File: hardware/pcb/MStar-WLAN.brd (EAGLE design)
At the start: 73.7 x 53.7 mm, 41 parts, among them J1 6P6C, J3 ZX62R-B-5P(30), Q1 VP2106, Q2 2N3904

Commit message: pcb
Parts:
- removed 3.3--5V: (no value), jumper:SJ_2
- removed D3: (no value), diode:D-5
- removed R8, R9: 10K, rcl:0207/2V
- C1: value 470u/25 -> 2m/25; device rcl:E3,5-8 -> rcl:E5-10,5
- C2: value 1m/6.3 -> 100u/6.3; device rcl:E5-10,5 -> rcl:E2,5-6
- moved C9 7.18 mm to (38.1, 10.2), turned to 90 degrees
- moved R4 5.24 mm to (49.5, 10.2)
- moved R7 5.24 mm to (41.9, 10.2)
- moved R3 5.08 mm to (53.3, 10.2)
- moved C10 5.08 mm to (45.7, 10.2)
- moved C1 4.02 mm to (19.1, 6.35)
- moved C2 2.84 mm to (33.7, 10.2)
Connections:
- removed net N$16: 3.3--5V.1, D3.A
- removed net N$20: 3.3--5V.2, C2.+, C3.1, OKI-78SR-3.3.OUT
- removed net N$8: ESP32-WROVER-B.4, R8.1, R9.2
- net GND: no longer R9.1
- net N$17: no longer D3.C
- net VCC: now also C2.+, C3.1, OKI-78SR-3.3.OUT; no longer 3.3--5V.3, R8.2
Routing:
- net N$20: track 50.7 -> 0.00 mm
- net N$8: track 20.9 -> 0.00 mm
- net N$16: track 16.5 -> 0.00 mm
- net ESP32_EN: track 82.6 -> 69.8 mm
- net TXD: track 44.3 -> 37.8 mm
- net N$2: track 110.7 -> 115.5 mm
- net N$7: track 14.0 -> 9.23 mm
- net VCC: track 191.4 -> 195.3 mm
- net SQW: track 114.3 -> 117.3 mm
- net N$4: track 7.86 -> 4.96 mm
- net RAW12: track 19.9 -> 17.7 mm
- net GND: track 1.74 -> 3.78 mm, vias 8 -> 10
- net N$17: track 9.81 -> 7.91 mm
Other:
- board text added: "MStar-WLAN mjs 2019.12"
- board text removed: "MStar-WLAN mjs 2019.5"

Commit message: ESP32 work
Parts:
- added C11: 10u, rcl:C1206
- added SD: (no value), con-lsta:FE06
- moved R1 8.08 mm to (5.71, 36.8), turned to 180 degrees
- moved Q1 4.07 mm to (50.2, 45.7)
- moved Q2 4.07 mm to (43.8, 45.7)
- moved R2 1.27 mm to (40.6, 50.2)
- moved R5 1.27 mm to (53.3, 50.2)
- moved R6 1.27 mm to (47.0, 50.2)
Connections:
- new net N$16: ESP32-WROVER-B.29, SD.2
- new net N$20: ESP32-WROVER-B.30, SD.4
- new net N$22: ESP32-WROVER-B.37, SD.3
- new net N$8: ESP32-WROVER-B.31, SD.5
- net GND: now also C11.2, SD.6
- net RX_ENA: now also ESP32-WROVER-B.10; no longer ESP32-WROVER-B.37
- net VCC: now also C11.1, SD.1
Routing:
- net I2C_SCL: track 138.1 -> 63.8 mm, vias 1 -> 3
- net N$2: track 115.5 -> 67.1 mm
- net SQW: track 117.3 -> 85.3 mm
- net N$22: track 0.00 -> 21.0 mm
- net /MBUS: track 52.2 -> 72.9 mm
- net VCC: track 195.3 -> 175.9 mm
- net N$19: track 74.9 -> 61.6 mm, vias 0 -> 2
- net RX_ENA: track 45.3 -> 56.2 mm, vias 1 -> 2
- net N$16: track 0.00 -> 10.6 mm
- net ESP32_EN: track 69.8 -> 61.2 mm
- net RXD: track 52.8 -> 61.1 mm, vias 3 -> 2
- net N$13: track 15.8 -> 22.8 mm
- net N$20: track 0.00 -> 6.99 mm
- net N$8: track 0.00 -> 6.47 mm
- net /RTS: track 15.3 -> 9.87 mm
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
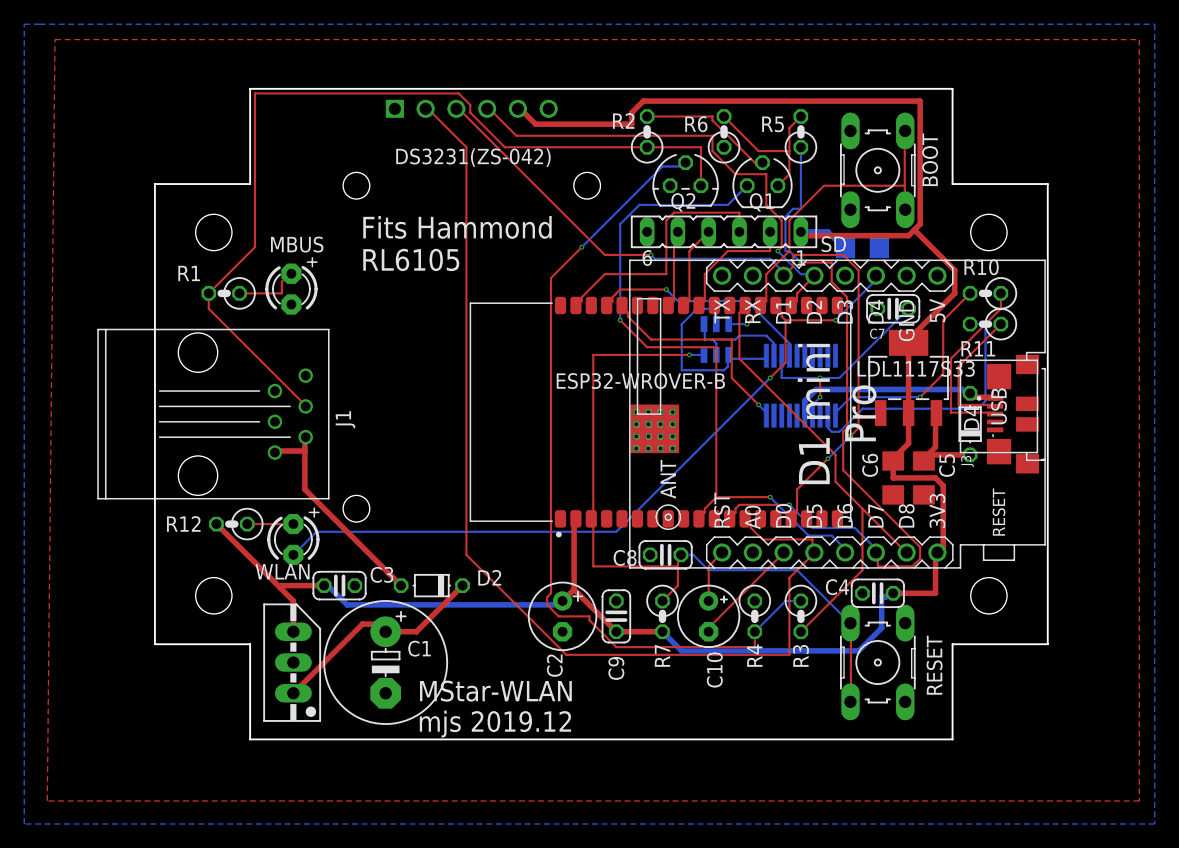
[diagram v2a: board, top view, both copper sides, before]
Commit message: bug fixes. SD Card support. New PCB.
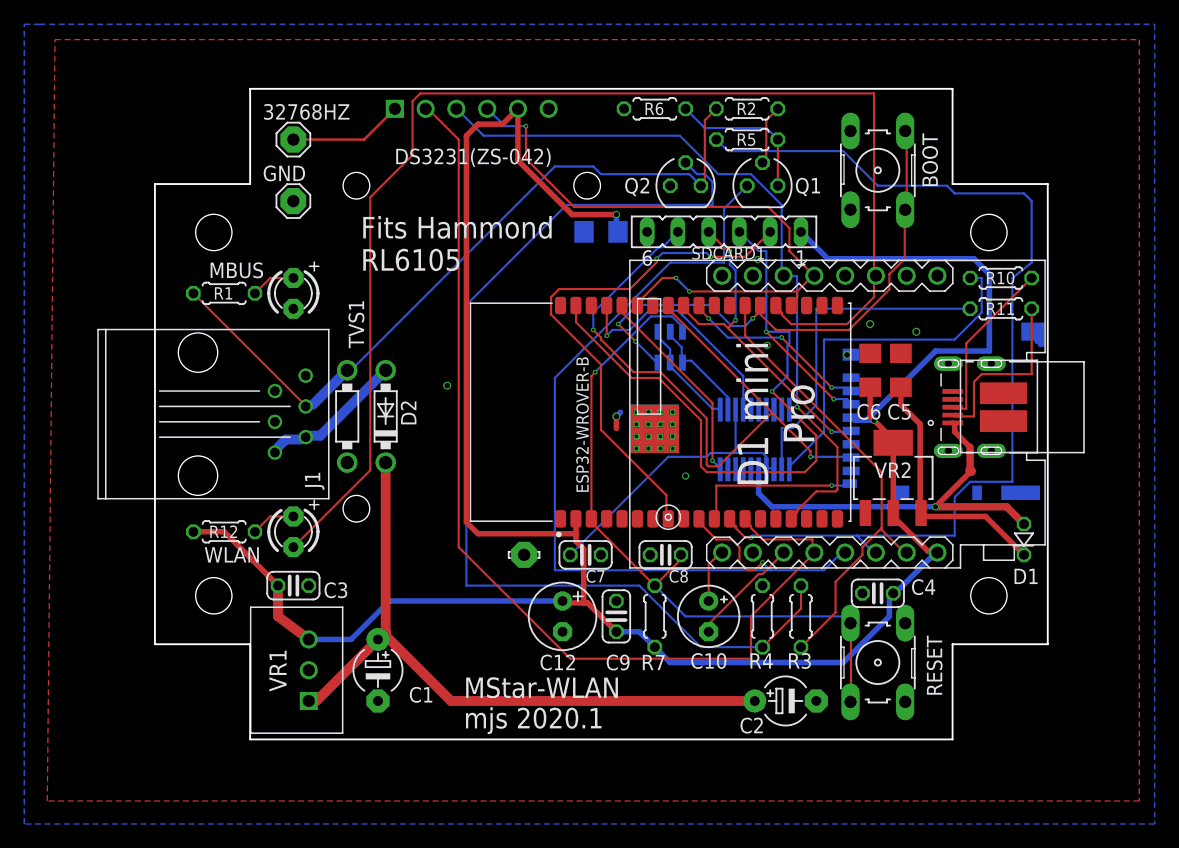
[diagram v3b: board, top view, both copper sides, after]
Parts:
- removed D4: (no value), diode:D-5
- removed J3: ZX62R-B-5P(30), MyLibrary:HRS_ZX62R-B-5P(30)
- removed LDL1117S33: (no value), MyLibrary:SOT223
- removed OKI-78SR-3.3: (no value), v-reg:78MXXS
- removed SD: (no value), con-lsta:FE06
- added 32768HZ, GND: MCS10B, MStar-WLAN:MCS10B
- added C12: 100u, MStar-WLAN:E2,5-6
- added D1: SB140-E3, MStar-WLAN:D-2.5
- added J2: UJ2-MIBH-4-SMT, MStar-WLAN:CUI_UJ2-MIBH-4-SMT
- added PAD: LSP10, MStar-WLAN:LSP10
- added SDCARD0: DM3BT-DSF-PEJS, MStar-WLAN:DM3BT-DSF-PEJS
- added SDCARD1: Card, MStar-WLAN:FE06
- added TVS1: TVS-, MStar-WLAN:DO41-7.6:1
- added VR1: VREG-OKI-78SR-3.3/1.5-W36, MStar-WLAN:OKI-78SR
- added VR2: LDL1117S33, MStar-WLAN:SOT223
- BOOT, RESET: device switch-omron:B3F-10XX -> MStar-WLAN:B3F-10XX
- C1: value 2m/25 -> 1.5/5; device rcl:E5-10,5 -> MStar-WLAN:E5-4
- C10: device rcl:E2,5-5 -> MStar-WLAN:E2,5-5
- C11, C5, C6: device rcl:C1206 -> MStar-WLAN:C1206
- C2: value 100u/6.3 -> 2m/25; device rcl:E2,5-6 -> MStar-WLAN:E5-4
- C3, C4, C7, C8, C9: device rcl:C025-024X044 -> MStar-WLAN:C025-024X044
- D2: value (none) -> SB140-E3; device diode:D-5 -> MStar-WLAN:DO41-7.6
- DS3231(ZS-042): value (none) -> RTC-DS3231-AT24C32-6; device MyLibrary:RTC-DS3231-AT24C32-6 -> MStar-WLAN:RTC-DS3231-AT24C32-6
- ESP32-WROVER-B: value (none) -> ESP32-WROVER-I; device MyLibrary:XCVR_ESP32-WROVER-I -> MStar-WLAN:XCVR_ESP32-WROVER-I
- FT231XS: device MyLibrary:SSOP20 -> MStar-WLAN:SSOP20
- IMH3A: value (none) -> IMH3ATSOP6; device MyLibrary:TSOP6 -> MStar-WLAN:TSOP6
- J1: device con-rj:RJ12 -> MStar-WLAN:RJ12
- MBUS, WLAN: device adafruit:LED3MM -> MStar-WLAN:LED3MM
- Q1: device MyLibrary:TO92 -> MStar-WLAN:TO92
- Q2: value 2N3904 -> 2N3904 or TN2106*; device transistor-small-signal:TO92D -> MStar-WLAN:TO92B
- R1, R10, R11, R12, R2, R4, R6: device rcl:0207/2V -> MStar-WLAN:0204/5
- R3, R5: value 1K -> 1k; device rcl:0207/2V -> MStar-WLAN:0204/5
- R7: value 27k -> 10k; device rcl:0207/2V -> MStar-WLAN:0204/5
- U$1: device MyLibrary:WEMOS-D1-MINI-PRO -> MStar-WLAN:WEMOS-D1-MINI-PRO
- moved C7 32.5 mm to (35.6, 15.2), turned to 0 degrees
- moved C11 21.6 mm to (36.8, 41.9), turned to 0 degrees
- moved C2 19.7 mm to (52.1, 3.17), turned to 0 degrees
- moved D2 14.5 mm to (19.1, 26.7), turned to 90 degrees
- moved C5 9.09 mm to (61.6, 30.5), turned to 90 degrees
- moved C6 9.09 mm to (59.1, 30.5), turned to 90 degrees
- moved R2 8.47 mm to (48.9, 52.1), turned to 0 degrees
- moved R6 6.02 mm to (41.3, 52.1), turned to 0 degrees
- moved FT231XS 5.85 mm to (49.5, 24.8)
- moved R5 4.49 mm to (48.9, 49.5), turned to 0 degrees
- moved IMH3A 3.86 mm to (42.5, 32.4), turned to 90 degrees
- moved C3 3.81 mm to (11.4, 12.7)
- moved R10 1.80 mm to (69.8, 38.1)
- moved R11 1.80 mm to (69.8, 35.6)
- moved C1 0.90 mm to (18.4, 5.71)
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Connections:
- net N$19 renamed WLAN_LED
- net N$4 renamed WEMOS_RST
- net N$5 renamed TXD0
- net N$6 renamed RXD0
- net N$7 renamed SELF_RESET
- removed net N$16: ESP32-WROVER-B.29, SD.2
- removed net N$20: ESP32-WROVER-B.30, SD.4
- removed net N$22: ESP32-WROVER-B.37, SD.3
- removed net N$8: ESP32-WROVER-B.31, SD.5
- new net CLK: ESP32-WROVER-B.30, SDCARD0.5, SDCARD1.4
- new net CS: ESP32-WROVER-B.29, SDCARD0.2
- new net MISO: ESP32-WROVER-B.31, SDCARD0.7, SDCARD1.5
- new net MOSI: ESP32-WROVER-B.37, SDCARD0.3, SDCARD1.3
- new net N$4: ESP32-WROVER-B.11, SDCARD0.CD
- new net N$5: 32768HZ.MP, DS3231(ZS-042).J1.1
- new net N$7: ESP32-WROVER-B.8, SDCARD1.2
- net /MBUS: now also TVS1.C
- net GND: now also C12.-, GND.MP, J2.5, J2.SH1, J2.SH2, J2.SH3, J2.SH4, J2.SH5, J2.SH6, PAD.MP, SDCARD0.6, SDCARD0.CGND1, SDCARD0.CGND2, SDCARD0.CGND3, SDCARD0.CGND4, SDCARD0.CGND5, SDCARD0.CGND6, SDCARD0.GND, SDCARD1.6, TVS1.A, VR1.2, VR2.1; no longer J3.5, J3.S1, J3.S2, J3.S3, J3.S6, LDL1117S33.1, OKI-78SR-3.3.GND, SD.6
- net I2C_SDA: now also ESP32-WROVER-B.33
- net N$10: now also J2.2; no longer J3.2
- net N$17: now also D1.C, VR2.3; no longer D4.C, LDL1117S33.3
- net N$9: now also J2.3; no longer J3.3
- net RAW12: now also C2.+, VR1.1; no longer OKI-78SR-3.3.IN
- net VCC: now also C12.+, SDCARD0.4, SDCARD1.1, VR1.3, VR2.2, VR2.4; no longer C2.+, LDL1117S33.2, LDL1117S33.4, OKI-78SR-3.3.OUT, SD.1
- net VUSB: now also D1.A, J2.1; no longer D4.A, J3.1
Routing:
- net MOSI: track 0.00 -> 62.7 mm, vias 0 -> 3
- net MISO: track 0.00 -> 55.7 mm, vias 0 -> 2
- net WLAN_LED: track 61.6 -> 106.1 mm, vias 2 -> 0
- net N$7: track 0.00 -> 43.1 mm, vias 0 -> 2
- net RAW12: track 18.6 -> 56.1 mm
- net CLK: track 0.00 -> 27.7 mm, vias 0 -> 3
- net VCC: track 175.9 -> 198.4 mm, vias 0 -> 2
- net RXD: track 61.1 -> 82.2 mm, vias 2 -> 1
- net N$22: track 21.0 -> 0.00 mm
- net RX_ENA: track 56.2 -> 74.5 mm, vias 2 -> 1
- net N$2: track 67.1 -> 84.6 mm, vias 1 -> 0
- net IO0: track 28.8 -> 45.8 mm, vias 1 -> 3
- net VUSB: track 17.8 -> 33.7 mm, vias 0 -> 1
- net CS: track 0.00 -> 15.8 mm, vias 0 -> 3
- net N$4: track 0.00 -> 13.9 mm, vias 0 -> 1
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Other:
- board text added: "MStar-WLAN mjs 2020.1"
- board text removed: "MStar-WLAN mjs 2019.12"

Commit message: ESP32. Logging. Dynamic status update. More.
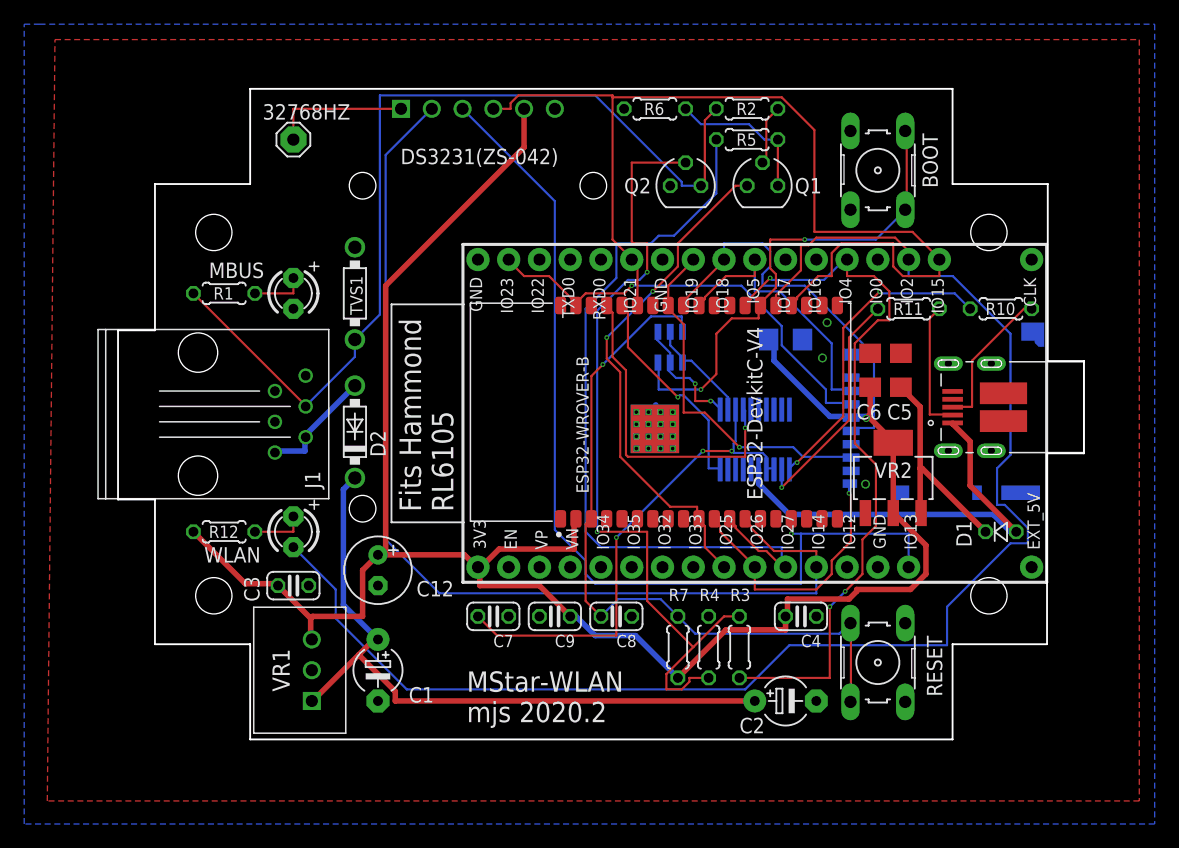
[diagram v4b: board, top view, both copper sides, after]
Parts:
- removed C11: 10u, MStar-WLAN:C1206
- removed GND: MCS10B, MStar-WLAN:MCS10B
- removed PAD: LSP10, MStar-WLAN:LSP10
- removed SDCARD1: Card, MStar-WLAN:FE06
- C1: value 1.5/5 -> 4m7/25
- C10: value 2.2u -> 10u; device MStar-WLAN:E2,5-5 -> MStar-WLAN:C1206
- C2: value 2m/25 -> 4m7/25
- Q2: value 2N3904 or TN2106* -> 2N3904 or TN0606
- R12: value 10k -> 1K
- U$1: value WEMOS-D1-MINI-PRO -> ESP32-DEVKITC-V4-NOSD; device MStar-WLAN:WEMOS-D1-MINI-PRO -> MStar-WLAN:ESP32-DEVKITC-V4-NOSD
- moved C10 23.7 mm to (52.1, 33.0), flipped to the bottom, turned to 180 degrees
- moved C12 15.7 mm to (18.4, 14.0)
- moved TVS1 10.2 mm to (16.5, 36.8), turned to 90 degrees
- moved C7 9.16 mm to (27.9, 10.2)
- moved R11 7.62 mm to (62.2, 35.6)
- moved U$1 6.83 mm to (49.5, 26.9), turned to 0 degrees
- moved C4 6.63 mm to (53.3, 10.2), turned to 0 degrees
- moved C8 6.51 mm to (38.1, 10.2), turned to 180 degrees
- moved R3 5.68 mm to (48.3, 7.62)
- moved R4 5.12 mm to (45.7, 7.62)
- moved C9 5.08 mm to (33.0, 10.2), turned to 180 degrees
- moved R7 3.18 mm to (43.2, 7.62)
- moved D2 2.84 mm to (16.5, 25.4)
- moved R10 2.54 mm to (69.8, 35.6)
- moved D1 2.01 mm to (69.8, 17.1), turned to 0 degrees
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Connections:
- removed net 5V: U$1.JP2.8
- removed net N$4: ESP32-WROVER-B.11, SDCARD0.CD
- removed net N$7: ESP32-WROVER-B.8, SDCARD1.2
- removed net SELF_RESET: C10.-, U$1.JP1.3
- removed net WEMOS_RST: C10.+, U$1.JP1.1
- new net CD: ESP32-WROVER-B.11, SDCARD0.CD, U$1.10
- new net EXT_5V: U$1.19
- net /DTR: now also IMH3A.1, IMH3A.5; no longer IMH3A.2, IMH3A.4
- net /RTS: now also IMH3A.2, IMH3A.4; no longer IMH3A.1, IMH3A.5
- net CLK: now also U$1.30; no longer SDCARD1.4
- net CS: now also U$1.29
- net ESP32_EN: now also IMH3A.3; no longer IMH3A.6
- net GND: now also C10.2, U$1.14, U$1.32, U$1.38; no longer C11.2, GND.MP, PAD.MP, SDCARD1.6, U$1.JP2.7
- net I2C_SCL: now also U$1.15; no longer U$1.JP2.3
- net I2C_SDA: now also U$1.23, U$1.33; no longer U$1.JP2.4
- net IO0: now also IMH3A.6; no longer IMH3A.3
- net MISO: now also U$1.31; no longer SDCARD1.5
- net MOSI: now also U$1.37; no longer SDCARD1.3
- net RXD: now also U$1.11; no longer U$1.JP1.6
- net RX_ENA: now also U$1.9; no longer U$1.JP1.5
- net SQW: now also U$1.12; no longer U$1.JP1.4
- net TXD: now also U$1.26; no longer U$1.JP1.7
- net VCC: now also C10.1, U$1.1; no longer C11.1, SDCARD1.1, U$1.JP1.8
- net WLAN_LED: now also U$1.24; no longer U$1.JP2.6
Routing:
- net N$7: track 43.1 -> 0.00 mm, vias 2 -> 0
- net VCC: track 198.4 -> 162.4 mm, vias 2 -> 1
- net RX_ENA: track 74.5 -> 42.2 mm, vias 1 -> 2
- net I2C_SDA: track 53.4 -> 85.5 mm, vias 3 -> 0
- net MISO: track 55.7 -> 29.4 mm, vias 2 -> 1
- net MOSI: track 62.7 -> 36.7 mm, vias 3 -> 1
- net CD: track 0.00 -> 22.3 mm, vias 0 -> 1
- net TXD: track 38.7 -> 59.1 mm, vias 0 -> 3
- net RXD: track 82.2 -> 64.2 mm, vias 1 -> 0
- net N$2: track 84.6 -> 66.9 mm, vias 0 -> 2
- net I2C_SCL: track 61.1 -> 78.5 mm
- net /MBUS: track 61.5 -> 78.0 mm
- net N$15: track 25.2 -> 41.1 mm, vias 0 -> 3
- net WLAN_LED: track 106.1 -> 120.8 mm
- net N$4: track 13.9 -> 0.00 mm, vias 1 -> 0
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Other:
- board size 73.7 x 53.7 mm -> 79.8 x 53.7 mm
- board text added: "MStar-WLAN mjs 2020.2"
- board text removed: "MStar-WLAN mjs 2020.1"

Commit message: Logging, hardware change to USB C
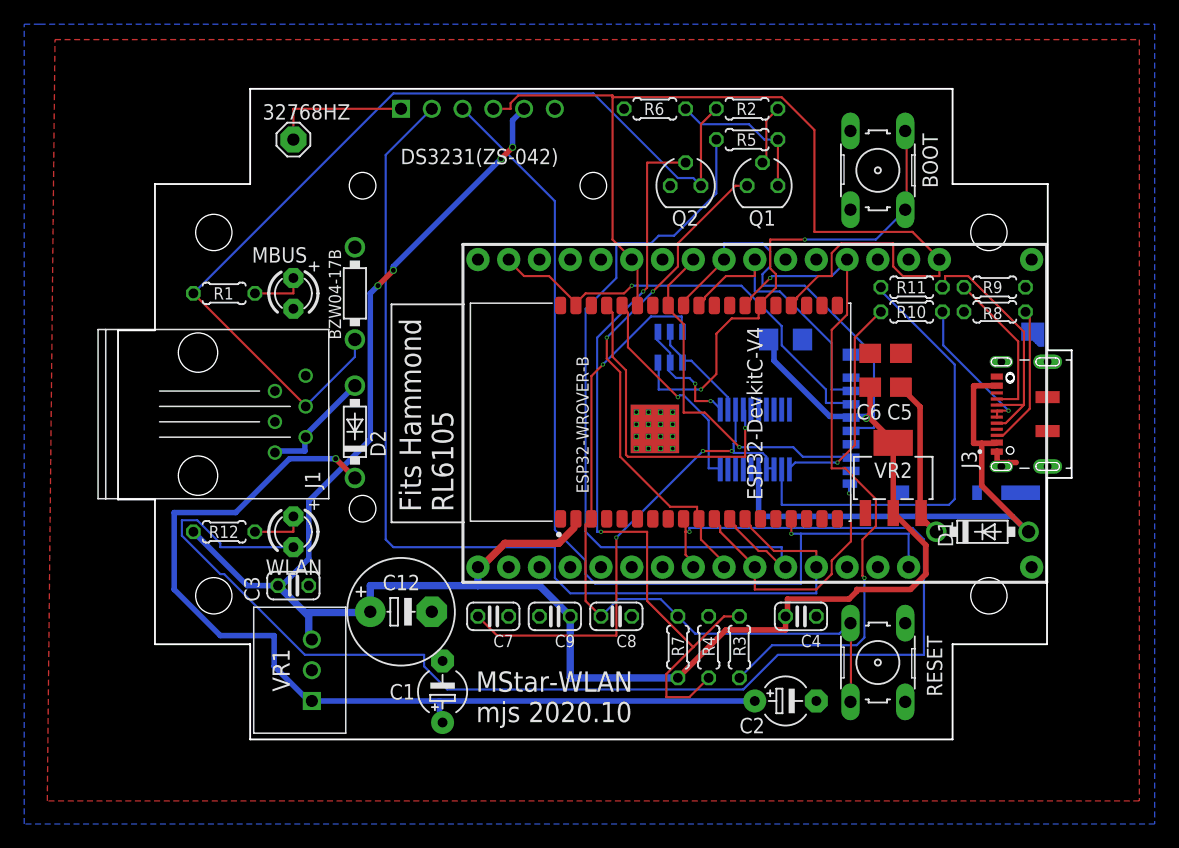
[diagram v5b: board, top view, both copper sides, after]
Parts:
- removed J2: UJ2-MIBH-4-SMT, MStar-WLAN:CUI_UJ2-MIBH-4-SMT
- added J3: DX07S016JA1R1500, MStar-WLAN:JAE_DX07S016JA1R1500
- added R8, R9: 5K1, MStar-WLAN:0204/5
- C12: device MStar-WLAN:E2,5-6 -> rcl:E5-8,5
- D1: device MStar-WLAN:D-2.5 -> MStar-WLAN:DO41-7.6
- J1: value 6P6C -> Kobiconn 154-UL6661
- Q2: value 2N3904 or TN0606 -> TN0606; device MStar-WLAN:TO92B -> MStar-WLAN:TO92
- R1, R7: value 10k -> 10K
- R2: value 10K -> 1K
- R3, R5: value 1k -> 1K
- moved R10 7.37 mm to (62.5, 35.3)
- moved C1 5.62 mm to (23.7, 3.94), turned to 90 degrees
- moved C12 3.92 mm to (20.3, 10.5), turned to 0 degrees
- moved R11 1.80 mm to (62.5, 37.3)
- moved D1 1.52 mm to (68.3, 17.1)
- renumbered TVS1 to BZW04-17B
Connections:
- net N$11 renamed USBDP
- net N$13 renamed USBDM
- removed net N$10: J2.2, R11.1
- removed net N$9: J2.3, R10.1
- removed net VUSB: D1.A, FT231XS.15, J2.1
- new net N$6: J3.9, R9.1
- new net N$7: J3.3, R8.1
- new net USBD+: J3.6, J3.7, R10.1
- new net USBD-: J3.5, J3.8, R11.1
- new net VBUS: D1.A, FT231XS.15, J3.11, J3.2
- net /MBUS: now also Q2.D; no longer Q2.C
- net GND: now also J3.1, J3.12, J3.S1, J3.S2, J3.S3, J3.S4, J3.S5, J3.S6, Q2.S, R8.2, R9.2; no longer J2.5, J2.SH1, J2.SH2, J2.SH3, J2.SH4, J2.SH5, J2.SH6, Q2.E
- net N$2: now also Q2.G; no longer Q2.B
- net WLAN_LED: now also ESP32-WROVER-B.9, U$1.8; no longer ESP32-WROVER-B.24, U$1.24
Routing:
- net VBUS: track 0.00 -> 44.2 mm
- net VUSB: track 35.3 -> 0.00 mm
- net RAW12: track 57.2 -> 78.9 mm, vias 0 -> 1
- net USBD-: track 0.00 -> 20.6 mm
- net USBDM: track 19.6 -> 37.4 mm, vias 1 -> 0
- net N$6: track 0.00 -> 12.9 mm
- net N$9: track 12.1 -> 0.00 mm
- net N$7: track 0.00 -> 12.0 mm
- net USBD+: track 0.00 -> 11.9 mm, vias 0 -> 1
- net N$10: track 11.0 -> 0.00 mm
- net USBDP: track 25.9 -> 18.2 mm, vias 2 -> 1
- net WLAN_LED: track 120.8 -> 114.1 mm, vias 0 -> 1
- net VCC: track 162.4 -> 168.6 mm, vias 1 -> 5
- net N$17: track 18.7 -> 13.2 mm
- net TXD: track 59.1 -> 56.3 mm, vias 3 -> 2
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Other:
- board size 79.8 x 53.7 mm -> 78.7 x 53.7 mm
- board text added: "MStar-WLAN mjs 2020.10"
- board text removed: "MStar-WLAN mjs 2020.2"
